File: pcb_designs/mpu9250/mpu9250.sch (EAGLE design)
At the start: 2 parts

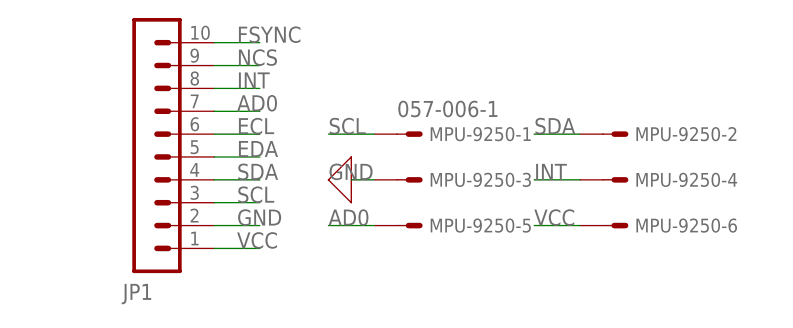
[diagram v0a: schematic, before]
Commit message: Added BNO055 MPU files
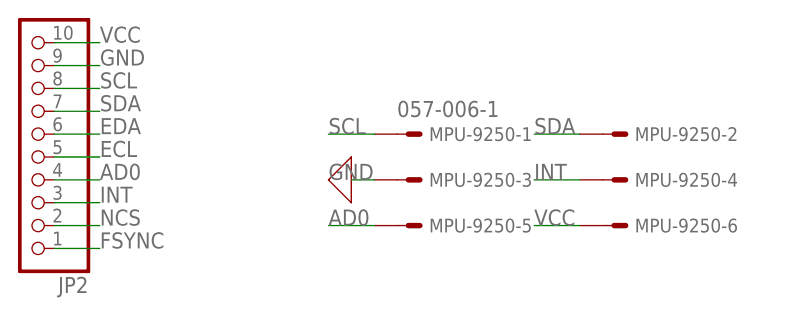
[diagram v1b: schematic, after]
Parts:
- removed JP1: (no value), con-lstb:MA10-1
- added JP2: (no value), pinhead:PINHD-1X10
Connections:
- net AD0: now also JP2.4; no longer JP1.7
- net ECL: now also JP2.5; no longer JP1.6
- net EDA: now also JP2.6; no longer JP1.5
- net FSYNC: now also JP2.1; no longer JP1.10
- net GND: now also JP2.9; no longer JP1.2
- net INT: now also JP2.3; no longer JP1.8
- net NCS: now also JP2.2; no longer JP1.9
- net SCL: now also JP2.8; no longer JP1.3
- net SDA: now also JP2.7; no longer JP1.4
- net VCC: now also JP2.10; no longer JP1.1
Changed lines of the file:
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@@
 </classes>
 <parts>
-<part name="JP1" library="con-lstb" library_urn="urn:adsk.eagle:library:162" deviceset="MA10-1" device="" package3d_urn="urn:adsk.eagle:package:8346/1"/>
 <part name="MPU-9250" library="con-panduit" library_urn="urn:adsk.eagle:library:169" deviceset="057-006-" device="1" package3d_urn="urn:adsk.eagle:package:9198/1"/>
 <part name="X_3" library="ngspice-simulation" library_urn="urn:adsk.eagle:library:527439" deviceset="GND" device=""/>
+<part name="JP2" library="pinhead" library_urn="urn:adsk.eagle:library:325" deviceset="PINHD-1X10" device="" package3d_urn="urn:adsk.eagle:package:22406/2"/>
 </parts>
 <sheets>
@@
 </plain>
 <instances>
-<instance part="JP1" gate="1" x="182.88" y="33.02" smashed="yes">
-<attribute name="NAME" x="180.34" y="17.145" size="1.778" layer="95"/>
-<attribute name="VALUE" x="176.53" y="20.32" size="1.778" layer="96"/>
-</instance>
 <instance part="MPU-9250" gate="-1" x="213.36" y="35.56" smashed="yes">
 <attribute name="NAME" x="214.376" y="34.798" size="1.524" layer="95"/>
@@
 </instance>
 <instance part="X_3" gate="G$1" x="205.74" y="30.48" smashed="yes" rot="MR90"/>
+<instance part="JP2" gate="A" x="170.18" y="33.02" smashed="yes" rot="R180">
+<attribute name="NAME" x="176.53" y="19.685" size="1.778" layer="95" rot="R180"/>
+<attribute name="VALUE" x="176.53" y="50.8" size="1.778" layer="96" rot="R180"/>
+</instance>
 </instances>
 <busses>
@@
 <net name="VCC" class="0">
 <segment>
-<pinref part="JP1" gate="1" pin="1"/>
-<wire x1="190.5" y1="22.86" x2="195.58" y2="22.86" width="0.1524" layer="91"/>
-<label x="193.04" y="22.86" size="1.778" layer="95"/>
-</segment>
-<segment>
 <pinref part="MPU-9250" gate="-6" pin="S"/>
 <wire x1="231.14" y1="25.4" x2="226.06" y2="25.4" width="0.1524" layer="91"/>
 <label x="226.06" y="25.4" size="1.778" layer="95"/>
 </segment>
+<segment>
+<pinref part="JP2" gate="A" pin="10"/>
+<wire x1="172.72" y1="45.72" x2="177.8" y2="45.72" width="0.1524" layer="91"/>
+<label x="177.8" y="45.72" size="1.778" layer="95"/>
+</segment>
 </net>
 <net name="GND" class="0">
-<segment>
-<pinref part="JP1" gate="1" pin="2"/>
-<wire x1="190.5" y1="25.4" x2="195.58" y2="25.4" width="0.1524" layer="91"/>
-<label x="193.04" y="25.4" size="1.778" layer="95"/>
-</segment>
 <segment>
 <pinref part="X_3" gate="G$1" pin="0"/>
@@
 <wire x1="205.74" y1="30.48" x2="208.28" y2="30.48" width="0.1524" layer="91"/>
 </segment>
+<segment>
+<pinref part="JP2" gate="A" pin="9"/>
+<wire x1="172.72" y1="43.18" x2="177.8" y2="43.18" width="0.1524" layer="91"/>
+<label x="177.8" y="43.18" size="1.778" layer="95"/>
+</segment>
 </net>
 <net name="SCL" class="0">
-<segment>
-<pinref part="JP1" gate="1" pin="3"/>
-<wire x1="190.5" y1="27.94" x2="195.58" y2="27.94" width="0.1524" layer="91"/>
-<label x="193.04" y="27.94" size="1.778" layer="95"/>
-</segment>
 <segment>
 <pinref part="MPU-9250" gate="-1" pin="S"/>
@@
 <label x="203.2" y="35.56" size="1.778" layer="95"/>
 </segment>
+<segment>
+<pinref part="JP2" gate="A" pin="8"/>
+<wire x1="172.72" y1="40.64" x2="177.8" y2="40.64" width="0.1524" layer="91"/>
+<label x="177.8" y="40.64" size="1.778" layer="95"/>
+</segment>
 </net>
 <net name="SDA" class="0">
-<segment>
-<pinref part="JP1" gate="1" pin="4"/>
-<wire x1="190.5" y1="30.48" x2="195.58" y2="30.48" width="0.1524" layer="91"/>
-<label x="193.04" y="30.48" size="1.778" layer="95"/>
-</segment>
 <segment>
 <pinref part="MPU-9250" gate="-2" pin="S"/>
@@
 <label x="226.06" y="35.56" size="1.778" layer="95"/>
 </segment>
+<segment>
+<pinref part="JP2" gate="A" pin="7"/>
+<wire x1="172.72" y1="38.1" x2="177.8" y2="38.1" width="0.1524" layer="91"/>
+<label x="177.8" y="38.1" size="1.778" layer="95"/>
+</segment>
 </net>
 <net name="EDA" class="0">
 <segment>
-<pinref part="JP1" gate="1" pin="5"/>
-<wire x1="190.5" y1="33.02" x2="195.58" y2="33.02" width="0.1524" layer="91"/>
-<label x="193.04" y="33.02" size="1.778" layer="95"/>
+<pinref part="JP2" gate="A" pin="6"/>
+<wire x1="172.72" y1="35.56" x2="177.8" y2="35.56" width="0.1524" layer="91"/>
+<label x="177.8" y="35.56" size="1.778" layer="95"/>
 </segment>
 </net>
 <net name="ECL" class="0">
 <segment>
-<pinref part="JP1" gate="1" pin="6"/>
-<wire x1="190.5" y1="35.56" x2="195.58" y2="35.56" width="0.1524" layer="91"/>
-<label x="193.04" y="35.56" size="1.778" layer="95"/>
+<pinref part="JP2" gate="A" pin="5"/>
+<wire x1="172.72" y1="33.02" x2="177.8" y2="33.02" width="0.1524" layer="91"/>
+<label x="177.8" y="33.02" size="1.778" layer="95"/>
 </segment>
 </net>
 <net name="AD0" class="0">
-<segment>
-<pinref part="JP1" gate="1" pin="7"/>
-<wire x1="190.5" y1="38.1" x2="195.58" y2="38.1" width="0.1524" layer="91"/>
-<label x="193.04" y="38.1" size="1.778" layer="95"/>
-</segment>
 <segment>
 <pinref part="MPU-9250" gate="-5" pin="S"/>
@@
 <label x="203.2" y="25.4" size="1.778" layer="95"/>
 </segment>
+<segment>
+<pinref part="JP2" gate="A" pin="4"/>
+<wire x1="172.72" y1="30.48" x2="177.8" y2="30.48" width="0.1524" layer="91"/>
+<label x="177.8" y="30.48" size="1.778" layer="95"/>
+</segment>
 </net>
 <net name="INT" class="0">
-<segment>
-<pinref part="JP1" gate="1" pin="8"/>
-<wire x1="190.5" y1="40.64" x2="195.58" y2="40.64" width="0.1524" layer="91"/>
-<label x="193.04" y="40.64" size="1.778" layer="95"/>
-</segment>
 <segment>
 <pinref part="MPU-9250" gate="-4" pin="S"/>
@@
 <label x="226.06" y="30.48" size="1.778" layer="95"/>
 </segment>
+<segment>
+<pinref part="JP2" gate="A" pin="3"/>
+<wire x1="172.72" y1="27.94" x2="177.8" y2="27.94" width="0.1524" layer="91"/>
+<label x="177.8" y="27.94" size="1.778" layer="95"/>
+</segment>
 </net>
 <net name="NCS" class="0">
 <segment>
-<pinref part="JP1" gate="1" pin="9"/>
-<wire x1="190.5" y1="43.18" x2="195.58" y2="43.18" width="0.1524" layer="91"/>
-<label x="193.04" y="43.18" size="1.778" layer="95"/>
+<pinref part="JP2" gate="A" pin="2"/>
+<wire x1="172.72" y1="25.4" x2="177.8" y2="25.4" width="0.1524" layer="91"/>
+<label x="177.8" y="25.4" size="1.778" layer="95"/>
 </segment>
 </net>
 <net name="FSYNC" class="0">
 <segment>
-<pinref part="JP1" gate="1" pin="10"/>
-<wire x1="190.5" y1="45.72" x2="195.58" y2="45.72" width="0.1524" layer="91"/>
-<label x="193.04" y="45.72" size="1.778" layer="95"/>
+<pinref part="JP2" gate="A" pin="1"/>
+<wire x1="172.72" y1="22.86" x2="177.8" y2="22.86" width="0.1524" layer="91"/>
+<label x="177.8" y="22.86" size="1.778" layer="95"/>
 </segment>
 </net>
